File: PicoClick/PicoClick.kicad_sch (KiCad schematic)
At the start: 6 parts, among them J1 Conn_01x12_Socket, P1 CONN_8, P2 CONN_8, U1 SST26F064B

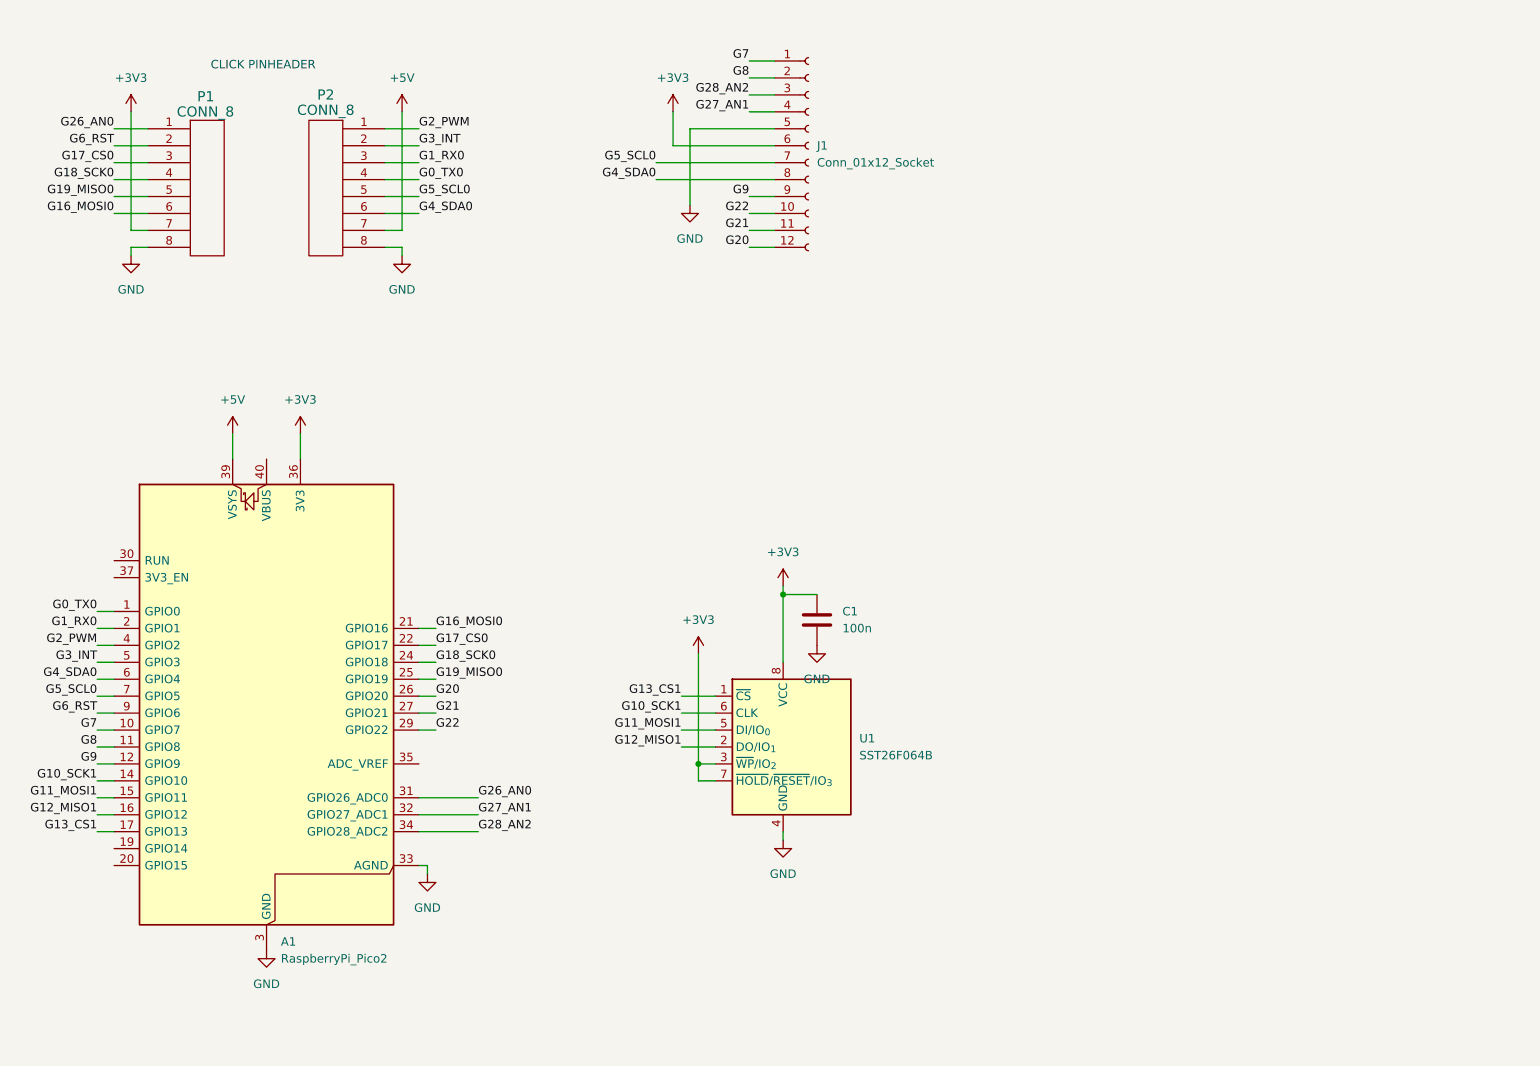
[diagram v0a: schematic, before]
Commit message: fix SPI labels
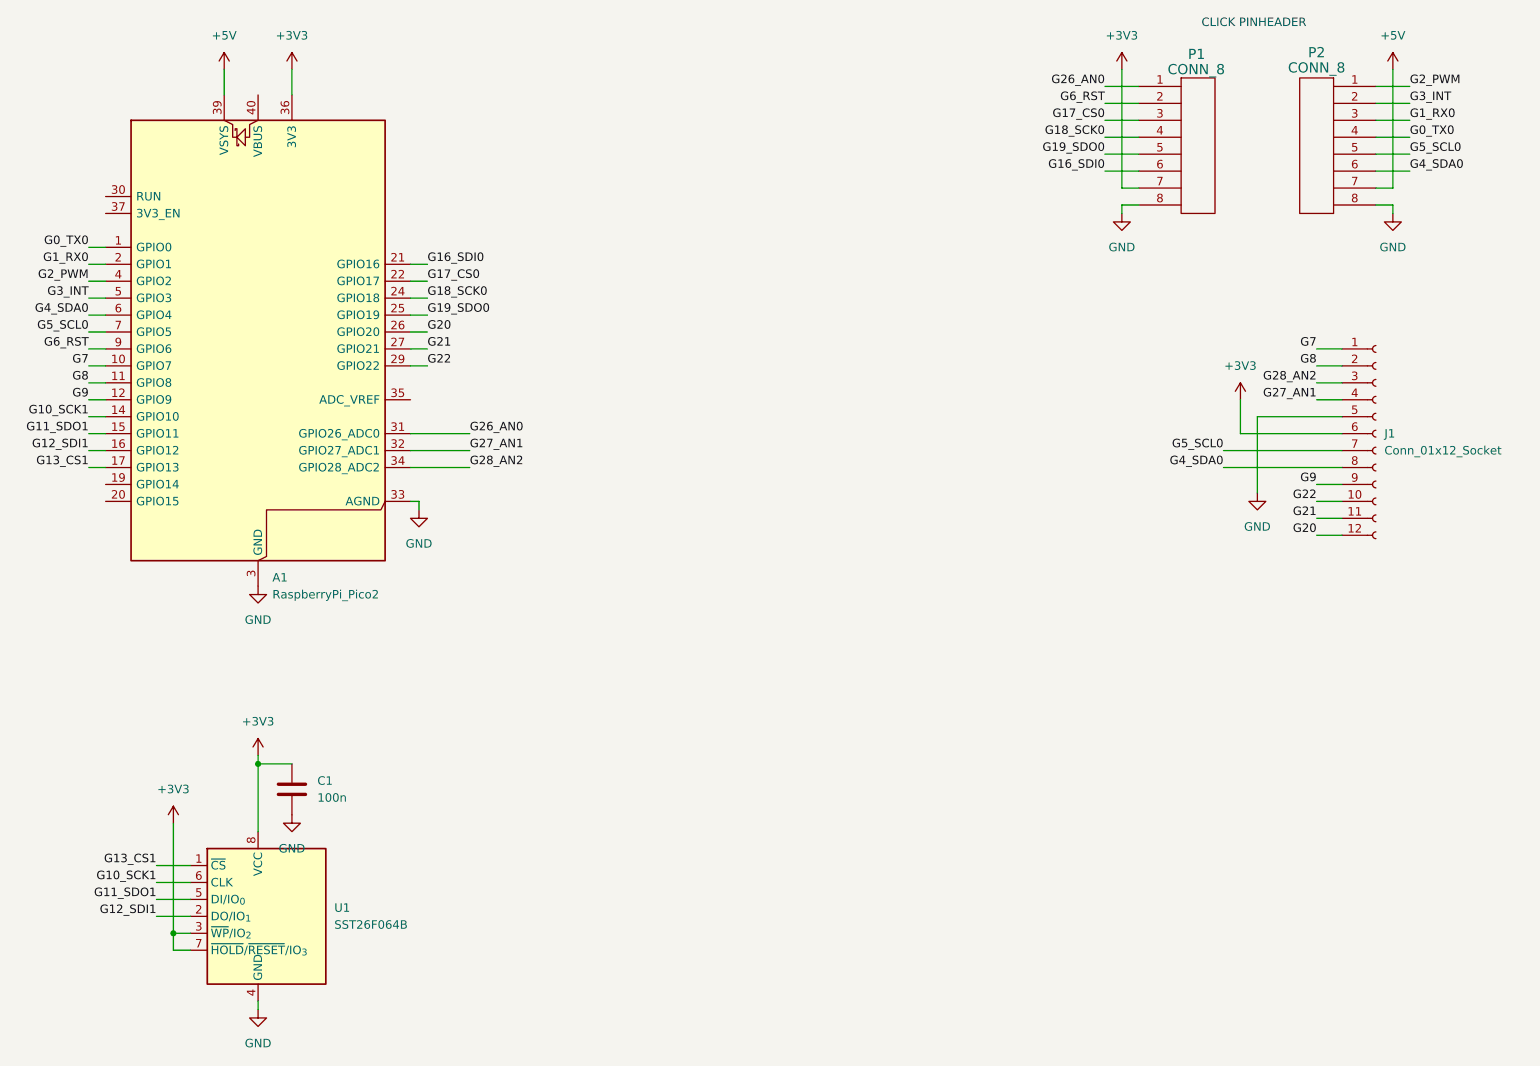
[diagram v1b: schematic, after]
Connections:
- net G11_MOSI1 renamed G11_SDO1
- net G12_MISO1 renamed G12_SDI1
- net G16_MOSI0 renamed G16_SDI0
- net G19_MISO0 renamed G19_SDO0
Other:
- moved on the sheet: A1, C1, J1, P1, P2, U1
